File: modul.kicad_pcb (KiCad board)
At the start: 2 copper layers, 40.1 x 43.9 mm, 9 parts, among them P1 CONN_6, T1 BT151-800r

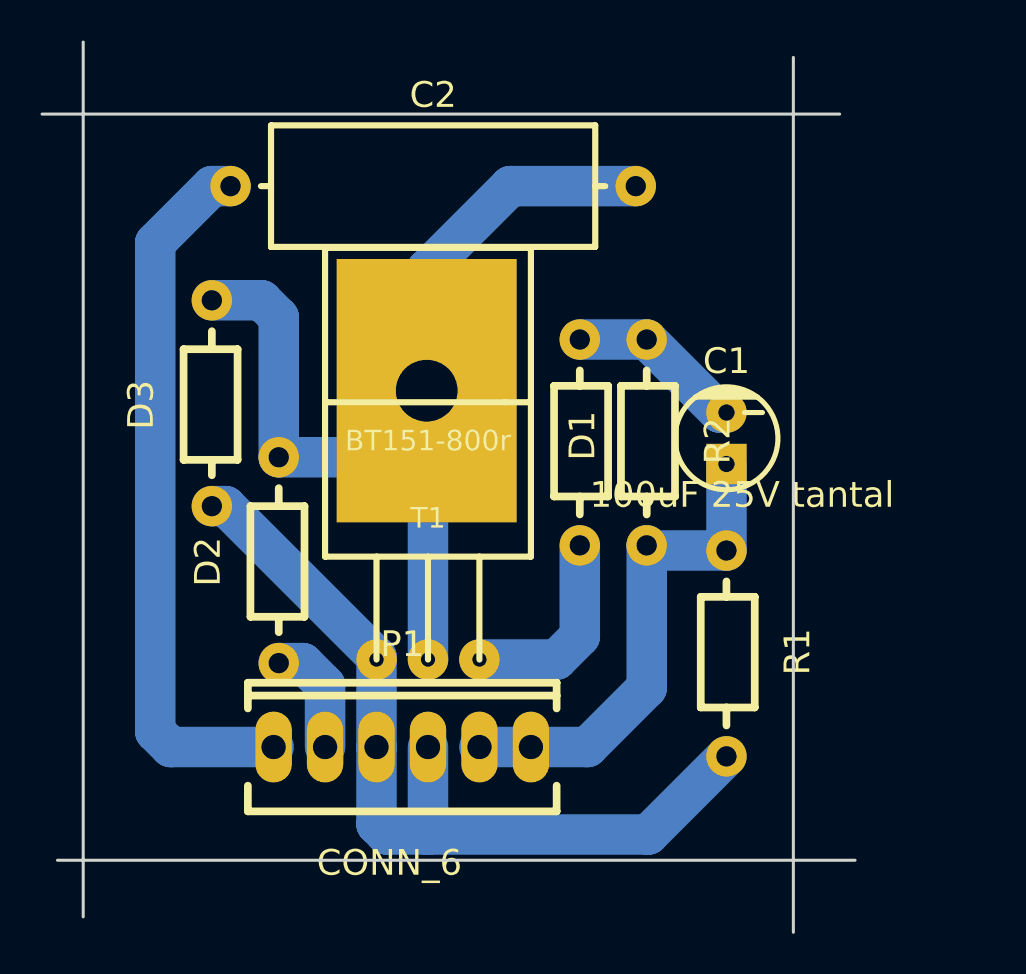
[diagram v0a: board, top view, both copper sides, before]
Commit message: project updated with photos, converted to kicad 7, cleaned form backups
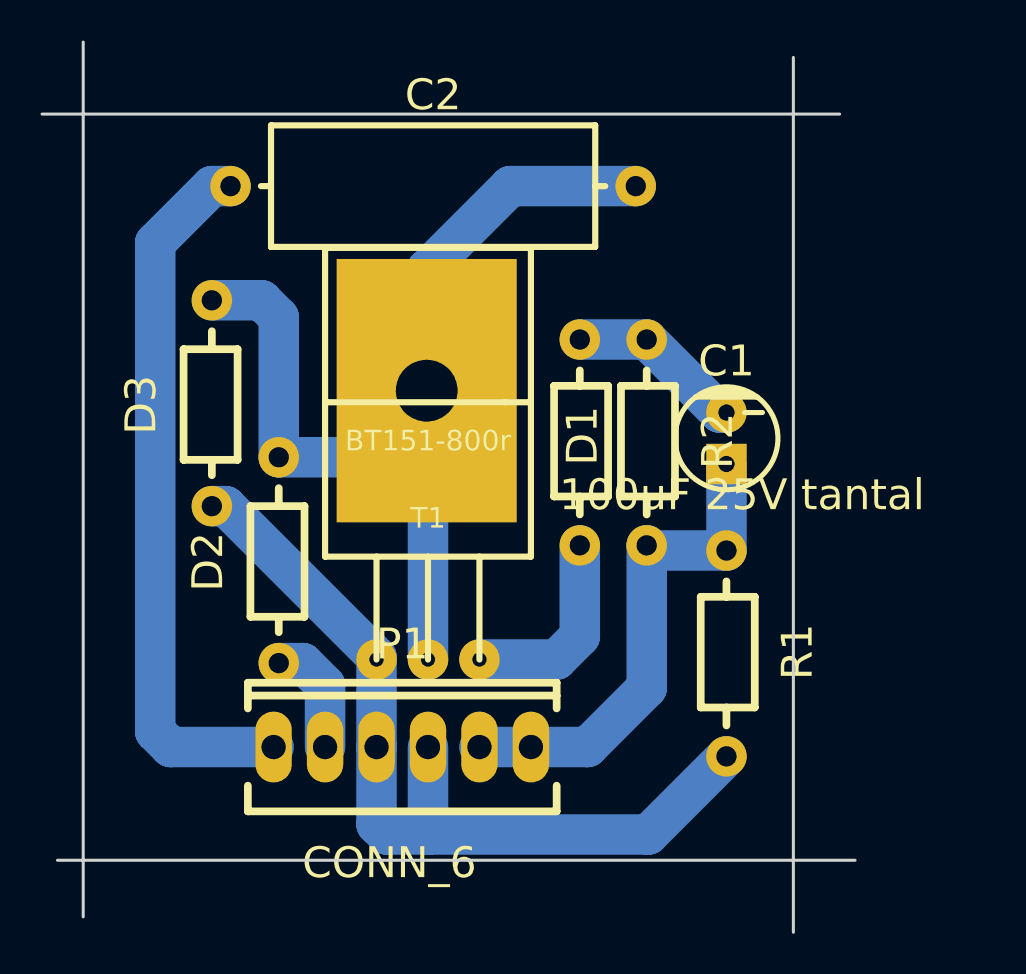
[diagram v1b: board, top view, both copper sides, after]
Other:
- net class Default removed
